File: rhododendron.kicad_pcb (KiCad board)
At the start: 2 copper layers, 73.7 x 53.3 mm, 55 parts, among them J1 Conn_02x20_Odd_Even, J2 Conn_02x20_Odd_Even, J7 BONUS_ROW, U1 USB3343, U2 M24C02-FMN

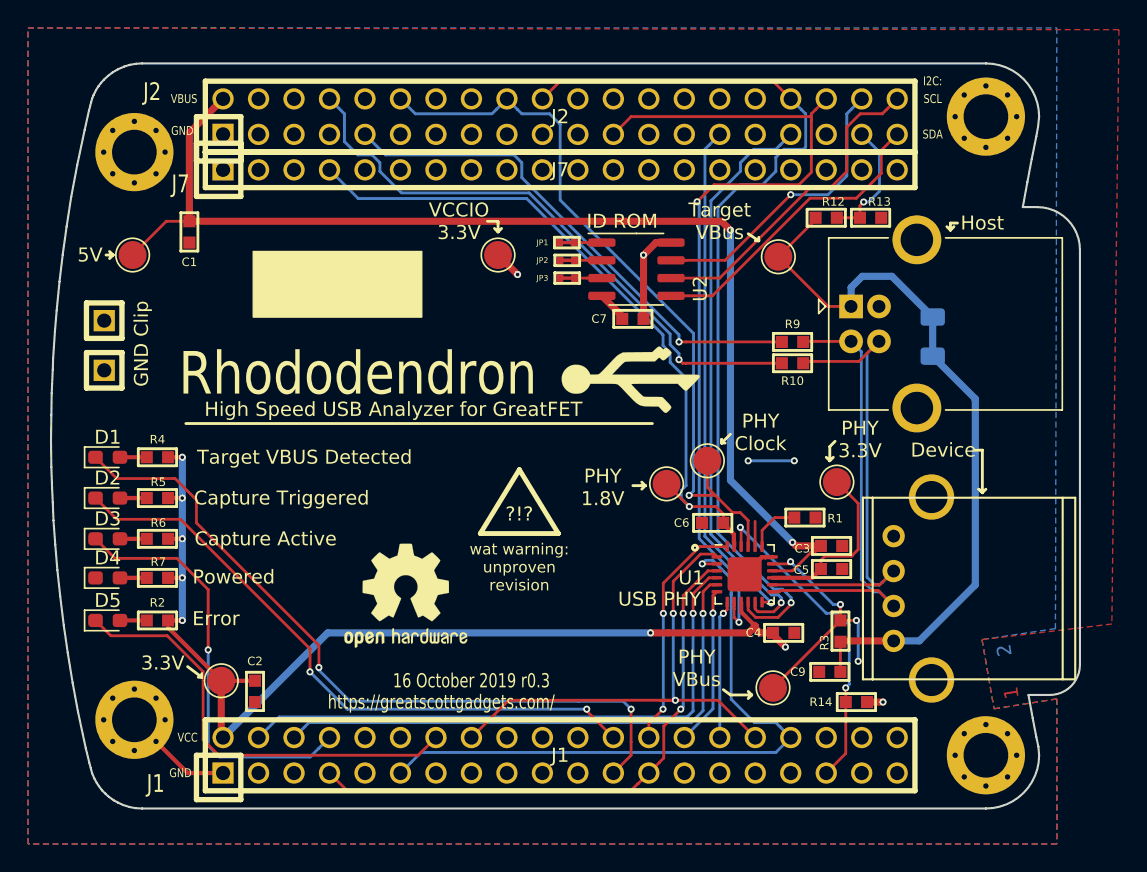
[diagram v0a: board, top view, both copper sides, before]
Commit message: r0.4: correct two "wasted" header pins (incorrectly connected to 3V3)
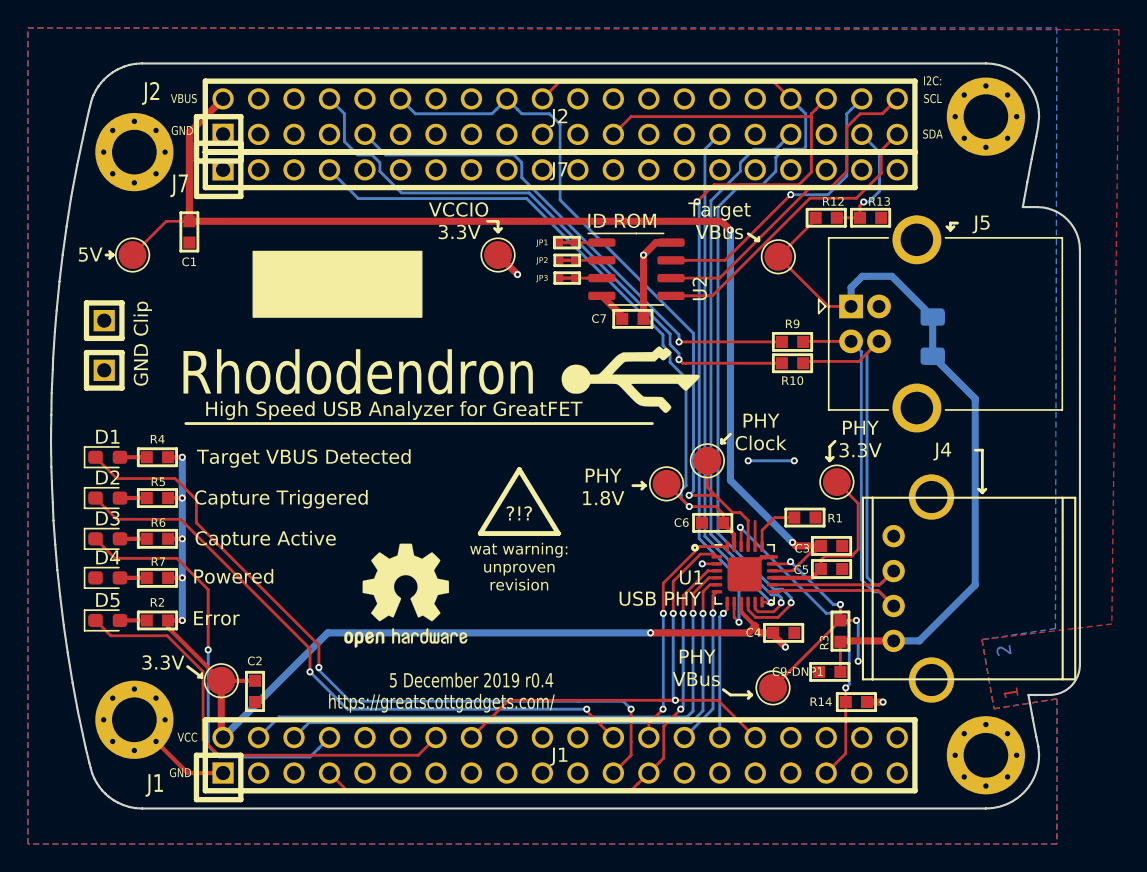
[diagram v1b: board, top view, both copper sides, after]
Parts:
- renumbered C9 to C9-DNP1, Device to J4, Host to J5, GND to TP10
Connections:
- J1 pad 11: +3V3 -> /CLK0
- J1 pad 34: +3V3 -> /P9_6
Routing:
- net +3V3: track 132.2 -> 86.3 mm
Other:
- board text added: "5 December 2019 r0.4"
- board text removed: "16 October 2019 r0.3"
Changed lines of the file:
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@@
-(kicad_pcb (version 20171130) (host pcbnew "(5.1.4-0-10_14)")
+(kicad_pcb (version 20171130) (host pcbnew "(5.1.2-1)-1")
   (general
     (thickness 1.6)
     (drawings 175)
-    (tracks 461)
+    (tracks 447)
     (zones 0)
     (modules 55)
-    (nets 105)
+    (nets 107)
   )
   (page A4)
   (layers
     (0 F.Cu signal)
-    (31 B.Cu signal hide)
+    (31 B.Cu signal)
     (32 B.Adhes user hide)
     (33 F.Adhes user hide)
@@
     (mod_text_width 0.15)
     (pad_size 1.524 1.524)
-    (pad_drill 0.762)
+    (pad_drill 1.016)
     (pad_to_mask_clearance 0.0508)
     (pad_to_paste_clearance_ratio -0.05)
@@
   (net 103 "Net-(JP3-Pad2)")
   (net 104 "Net-(U1-Pad20)")
+  (net 105 /P9_6)
+  (net 106 /CLK0)
   (net_class Default "This is the default net class."
     (clearance 0.2032)
@@
     (add_net /ADC0_0)
     (add_net /ADC0_2)
+    (add_net /CLK0)
     (add_net /I2C0_SCL)
     (add_net /I2C0_SDA)
@@
     (add_net /P7_7)
     (add_net /P9_5)
+    (add_net /P9_6)
     (add_net /PF_4)
     (add_net /PHY_VBUS)
@@
   (module gsg-modules:0603 (layer F.Cu)
     (at 165.354 112.141)
-    (fp_text reference C9 (at -2.286 0) (layer F.SilkS)
+    (fp_text reference C9-DNP1 (at -2.286 0) (layer F.SilkS)
       (effects (font (size 0.6096 0.6096) (thickness 0.1524)))
     )
@@
   (module rhododendron:CONN-Amphenol-UE27AC54100 (layer F.Cu)
     (at 169.926 106.172 90)
-    (fp_text reference Device (at 9.906 3.556 180) (layer F.SilkS)
+    (fp_text reference J4 (at 9.906 3.556 180) (layer F.SilkS)
       (effects (font (size 1 1) (thickness 0.15)))
     )
@@
     (descr "USB B receptacle, Horizontal, through-hole, http://www.on-shore.com/wp-content/uploads/2015/09/usb-b1hsxx.pdf")
     (tags "USB-B receptacle horizontal through-hole")
-    (fp_text reference Host (at 9.398 -5.969) (layer F.SilkS)
+    (fp_text reference J5 (at 9.398 -5.969) (layer F.SilkS)
       (effects (font (size 1 1) (thickness 0.15)))
     )
@@
       (net 29 /~PHY_RESET))
     (pad 34 thru_hole circle (at 16.51 -1.27) (size 1.524 1.524) (drill 1.016) (layers *.Cu *.Mask F.SilkS)
-      (net 92 +3V3))
+      (net 105 /P9_6))
     (pad 33 thru_hole circle (at 16.51 1.27) (size 1.524 1.524) (drill 1.016) (layers *.Cu *.Mask F.SilkS)
       (net 24 /P9_5))
@@
       (net 36 /P1_2))
     (pad 11 thru_hole circle (at -11.43 1.27) (size 1.524 1.524) (drill 1.016) (layers *.Cu *.Mask F.SilkS)
-      (net 92 +3V3))
+      (net 106 /CLK0))
     (pad 10 thru_hole circle (at -13.97 -1.27) (size 1.524 1.524) (drill 1.016) (layers *.Cu *.Mask F.SilkS)
       (net 37 /P1_1))
@@
     (at 113.411 90.551)
     (tags CONN)
-    (fp_text reference GND (at 0 2.286 180) (layer F.SilkS) hide
+    (fp_text reference TP10 (at 0 2.286 180) (layer F.SilkS) hide
       (effects (font (size 1.016 1.016) (thickness 0.2032)))
     )
@@
   (gr_line (start 109.6518 92.1766) (end 109.6264 93.726) (angle 90) (layer Edge.Cuts) (width 0.15))
   (gr_line (start 109.728 90.5002) (end 109.6518 92.1766) (angle 90) (layer Edge.Cuts) (width 0.15))
-  (gr_text "16 October 2019 r0.3" (at 139.7 112.776) (layer F.SilkS)
+  (gr_text "5 December 2019 r0.4" (at 139.7 112.776) (layer F.SilkS)
     (effects (font (size 1.016 0.762) (thickness 0.1524)))
   )
@@
   (segment (start 154.724452 99.148548) (end 155.067 98.806) (width 0.2032) (layer B.Cu) (net 4))
   (segment (start 155.295601 100.304601) (end 154.724452 99.733452) (width 0.2032) (layer B.Cu) (net 4))
-  (segment (start 160.008 103.1685) (end 160.008 101.358) (width 0.2032) (layer F.Cu) (net 104) (status 10))
   (segment (start 166.176 109.922) (end 166.116 109.982) (width 0.508) (layer F.Cu) (net 5) (status 30))
   (segment (start 169.926 109.922) (end 166.176 109.922) (width 0.508) (layer F.Cu) (net 5) (status 30))
@@
   (segment (start 114.54 99.695) (end 116.459 99.695) (width 0.3048) (layer F.Cu) (net 9))
   (segment (start 114.54 102.616) (end 116.459 102.616) (width 0.3048) (layer F.Cu) (net 10))
-  (segment (start 128.778001 117.601999) (end 129.54 116.84) (width 0.2032) (layer B.Cu) (net 93))
-  (segment (start 128.143 118.237) (end 128.778001 117.601999) (width 0.2032) (layer B.Cu) (net 93))
-  (segment (start 121.666 118.237) (end 128.143 118.237) (width 0.2032) (layer B.Cu) (net 93))
-  (segment (start 120.853199 117.424199) (end 121.666 118.237) (width 0.2032) (layer B.Cu) (net 93))
-  (segment (start 120.853199 110.566199) (end 120.853199 117.424199) (width 0.2032) (layer B.Cu) (net 93))
   (segment (start 114.54 105.41) (end 116.459 105.41) (width 0.3048) (layer F.Cu) (net 11))
-  (segment (start 157.2705 104.406) (end 156.222 104.406) (width 0.2032) (layer F.Cu) (net 92))
-  (via (at 156.222 104.406) (size 0.508) (drill 0.254) (layers F.Cu B.Cu) (net 92))
-  (segment (start 161.798001 116.078001) (end 162.56 116.84) (width 0.2032) (layer B.Cu) (net 92))
-  (segment (start 158.292801 114.096801) (end 159.969199 115.773199) (width 0.2032) (layer B.Cu) (net 92))
-  (segment (start 161.493199 115.773199) (end 161.798001 116.078001) (width 0.2032) (layer B.Cu) (net 92))
-  (segment (start 159.969199 115.773199) (end 161.493199 115.773199) (width 0.2032) (layer B.Cu) (net 92))
-  (segment (start 158.292801 105.467301) (end 158.292801 106.629199) (width 0.2032) (layer B.Cu) (net 92))
-  (segment (start 156.475999 104.152001) (end 156.977501 104.152001) (width 0.2032) (layer B.Cu) (net 92))
-  (segment (start 156.222 104.406) (end 156.475999 104.152001) (width 0.2032) (layer B.Cu) (net 92))
-  (segment (start 158.292801 106.476801) (end 158.292801 106.629199) (width 0.2032) (layer B.Cu) (net 92))
-  (segment (start 156.977501 104.152001) (end 158.292801 105.467301) (width 0.2032) (layer B.Cu) (net 92))
-  (segment (start 158.292801 106.629199) (end 158.292801 114.096801) (width 0.2032) (layer B.Cu) (net 92))
-  (segment (start 135.381999 118.618001) (end 134.62 119.38) (width 0.2032) (layer B.Cu) (net 92))
-  (segment (start 136.093199 117.906801) (end 135.381999 118.618001) (width 0.2032) (layer B.Cu) (net 92))
-  (segment (start 161.493199 117.906801) (end 136.093199 117.906801) (width 0.2032) (layer B.Cu) (net 92))
-  (segment (start 162.56 116.84) (end 161.493199 117.906801) (width 0.2032) (layer B.Cu) (net 92))
   (segment (start 154.858341 106.681159) (end 154.858341 107.950573) (width 0.2032) (layer F.Cu) (net 20))
   (segment (start 157.2705 104.906) (end 156.6335 104.906) (width 0.2032) (layer F.Cu) (net 20))
@@
   (segment (start 167.259 108.458) (end 166.116 108.458) (width 0.2032) (layer F.Cu) (net 91))
   (segment (start 166.116 108.458) (end 161.29 113.284) (width 0.2032) (layer F.Cu) (net 91))
+  (segment (start 157.2705 104.406) (end 156.222 104.406) (width 0.2032) (layer F.Cu) (net 92))
+  (via (at 156.222 104.406) (size 0.508) (drill 0.254) (layers F.Cu B.Cu) (net 92))
   (segment (start 159.008 107.852342) (end 160.02 108.864342) (width 0.3048) (layer F.Cu) (net 92))
   (segment (start 159.008 107.1435) (end 159.008 107.852342) (width 0.3048) (layer F.Cu) (net 92))
@@
   (segment (start 118.999 108.458) (end 118.999 105.41) (width 0.508) (layer B.Cu) (net 92))
   (segment (start 118.999 105.41) (end 118.999 96.774) (width 0.508) (layer B.Cu) (net 92))
+  (segment (start 128.778001 117.601999) (end 129.54 116.84) (width 0.2032) (layer B.Cu) (net 93))
+  (segment (start 128.143 118.237) (end 128.778001 117.601999) (width 0.2032) (layer B.Cu) (net 93))
+  (segment (start 121.666 118.237) (end 128.143 118.237) (width 0.2032) (layer B.Cu) (net 93))
+  (segment (start 120.853199 117.424199) (end 121.666 118.237) (width 0.2032) (layer B.Cu) (net 93))
+  (segment (start 120.853199 110.566199) (end 120.853199 117.424199) (width 0.2032) (layer B.Cu) (net 93))
   (via (at 120.853199 110.566199) (size 0.508) (drill 0.254) (layers F.Cu B.Cu) (net 93))
   (segment (start 120.853199 110.566199) (end 120.853199 106.248199) (width 0.2032) (layer F.Cu) (net 93))
@@
   (segment (start 147.961 83.947) (end 147.243801 83.947) (width 0.2032) (layer F.Cu) (net 103))
   (segment (start 149.036 83.947) (end 147.961 83.947) (width 0.2032) (layer F.Cu) (net 103))
+  (segment (start 160.008 103.1685) (end 160.008 101.358) (width 0.2032) (layer F.Cu) (net 104) (status 10))
   (zone (net 92) (net_name +3V3) (layer B.Cu) (hatch edge 0.508)
     (connect_pads (clearance 0.254))
